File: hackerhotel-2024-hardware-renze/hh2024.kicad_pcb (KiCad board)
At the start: 2 copper layers, 80 x 113 mm, 103 parts, among them J1 SAO, J2 Breakout pads, J3 Micro_SD_Card, J4 USB-C, J5 Battery, J6 E-Paper, K1 SANYOU_SRD_Form_C, Q1 AP2302B, Q2 AP2302B, Q3 AP2302B, SW1 Multi-Directional-Switches, SW2 Multi-Directional-Switches, SW3 Multi-Directional-Switches, SW4 Multi-Directional-Switches, SW5 Multi-Directional-Switches, SW6 SW_SPDT, U1 ESP32-C6-WROOM-1, U2 SY8079AAC, U3 XT4054K421MR-G, U4 SY6280AAC, U5 CH32V003F4U6

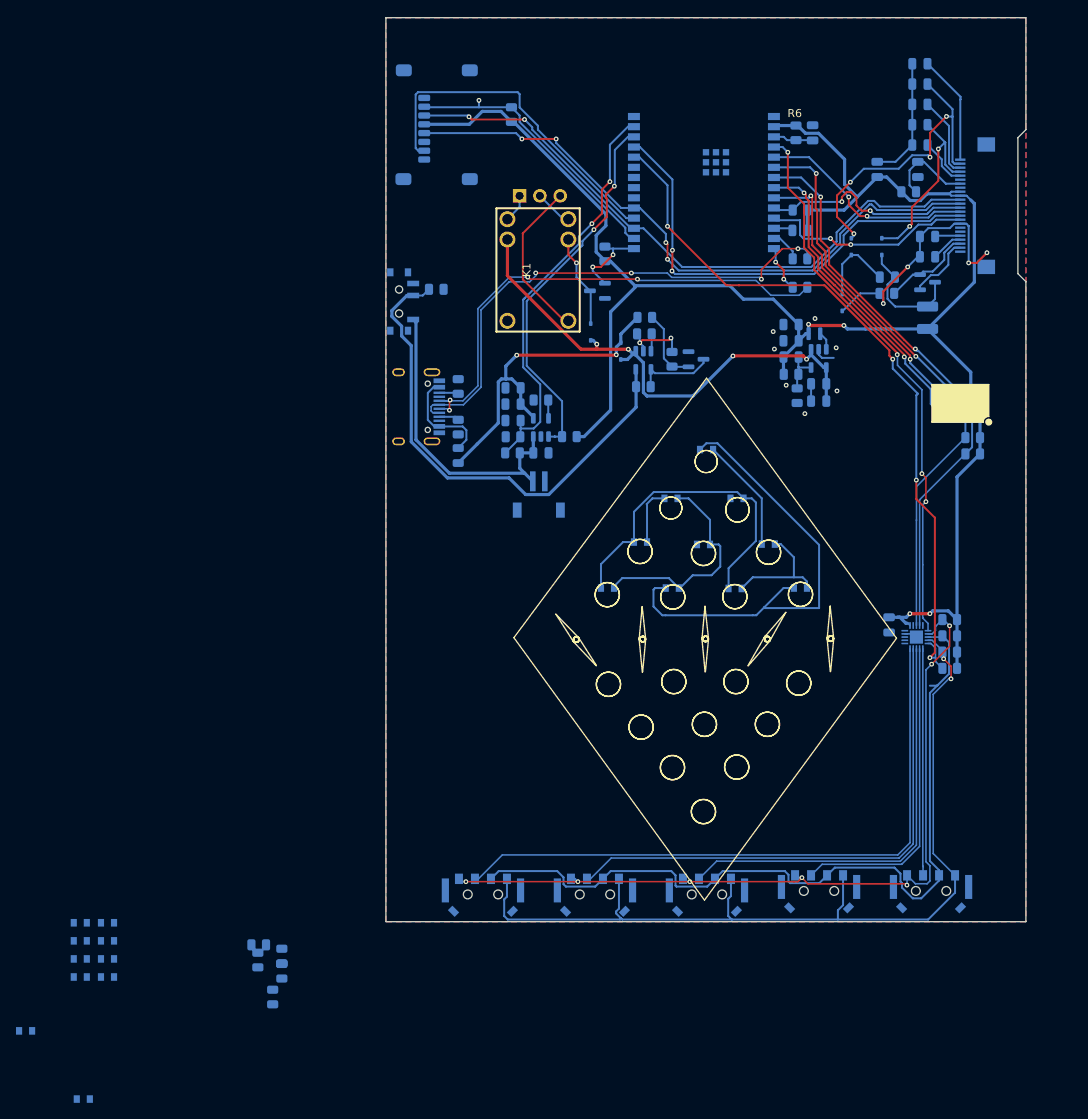
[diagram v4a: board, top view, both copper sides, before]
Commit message: Added artwork + more routing
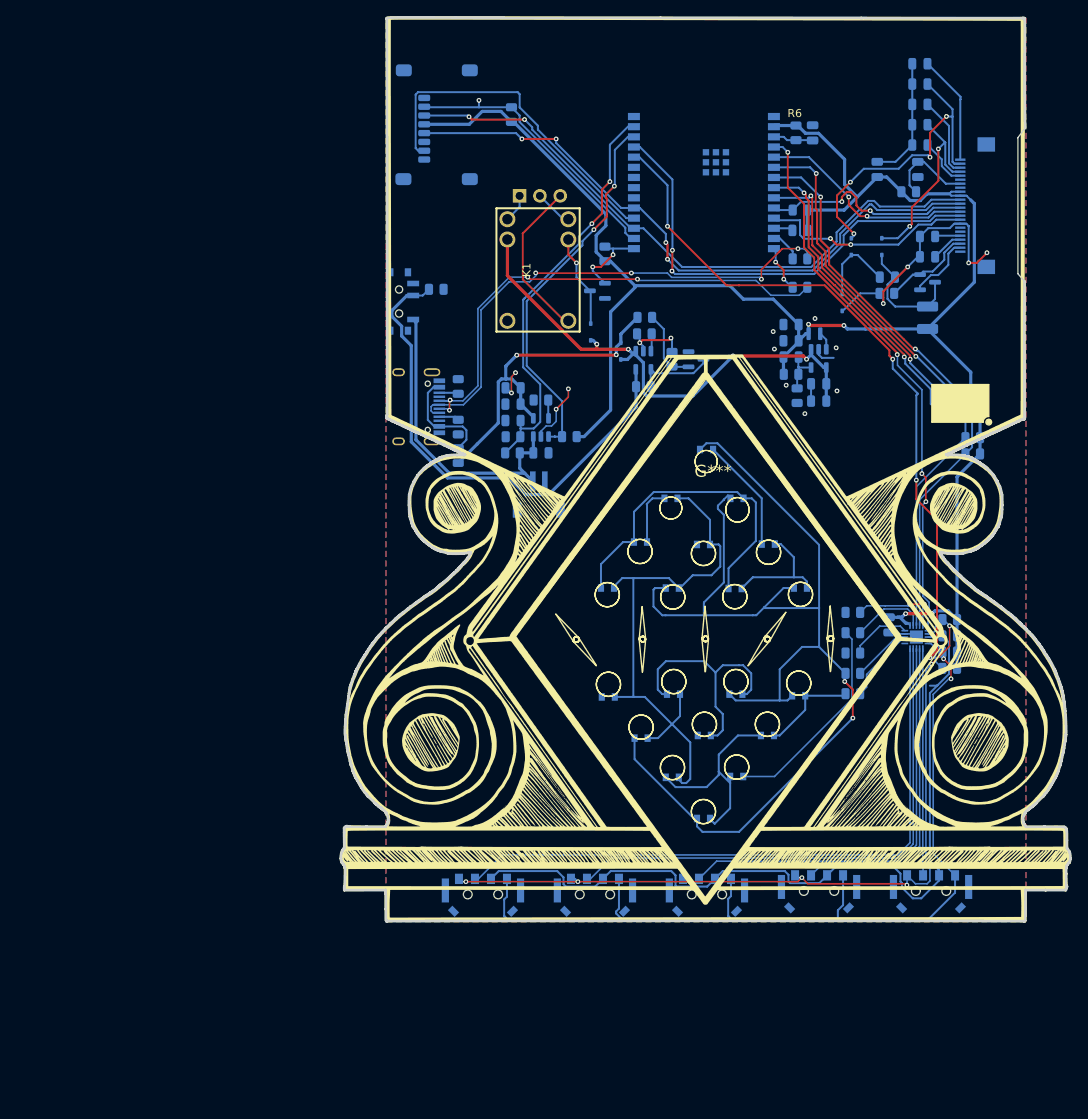
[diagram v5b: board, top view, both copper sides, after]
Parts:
- added G***: LOGO, HH2024Artwork:HH24_D2_F.SilkS, F.Cu at (132.9, 99.2)
- moved D20 98.3 mm to (135.8, 127.5)
- moved D17 91.7 mm to (143.6, 127.7)
- moved R24 86.1 mm to (150.4, 116.8), turned to 180 degrees
- moved D16 85.8 mm to (139.7, 132.7)
- moved D15 85.1 mm to (131.7, 143.1)
- moved R23 83.0 mm to (150.4, 124.5), turned to 180 degrees
- moved R26 83.0 mm to (150.4, 119.4), turned to 180 degrees
- moved D19 82.5 mm to (135.8, 137.8)
- moved R27 80.8 mm to (150.4, 121.9), turned to 180 degrees
- moved R25 80.6 mm to (150.4, 127.0)
- moved D18 79.7 mm to (131.8, 132.7)
- moved D21 79.5 mm to (128.0, 127.5)
- moved D23 77.4 mm to (127.8, 137.9)
- moved D24 76.2 mm to (123.9, 133.0)
- moved D22 72.7 mm to (119.8, 127.9)
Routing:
- net /E: track 58.4 -> 149.9 mm, vias 0 -> 2
- net /B: track 15.3 -> 71.7 mm
- net /A: track 27.7 -> 69.0 mm
- net /D: track 41.0 -> 67.2 mm
- net GND: track 65.1 -> 78.7 mm, vias 13 -> 17
- net /C: track 21.6 -> 33.8 mm
- net LED D: track 0.00 -> 11.2 mm, vias 0 -> 2
- net LED B: track 0.00 -> 9.52 mm
- net LED C: track 0.00 -> 9.28 mm
- net LED A: track 0.00 -> 7.75 mm
- net LED E: track 0.00 -> 7.46 mm
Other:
- board size 80 x 113 mm -> 91.2 x 113 mm
